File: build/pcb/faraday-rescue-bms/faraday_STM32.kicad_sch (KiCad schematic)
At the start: 58 parts, among them J1 532610571, J2 Conn_ARM_JTAG_SWD_10, J3 532610471, U2 STM32L010K8Tx, U4 THVD2410DR, Y1 ABS07-32.768KHZ-T

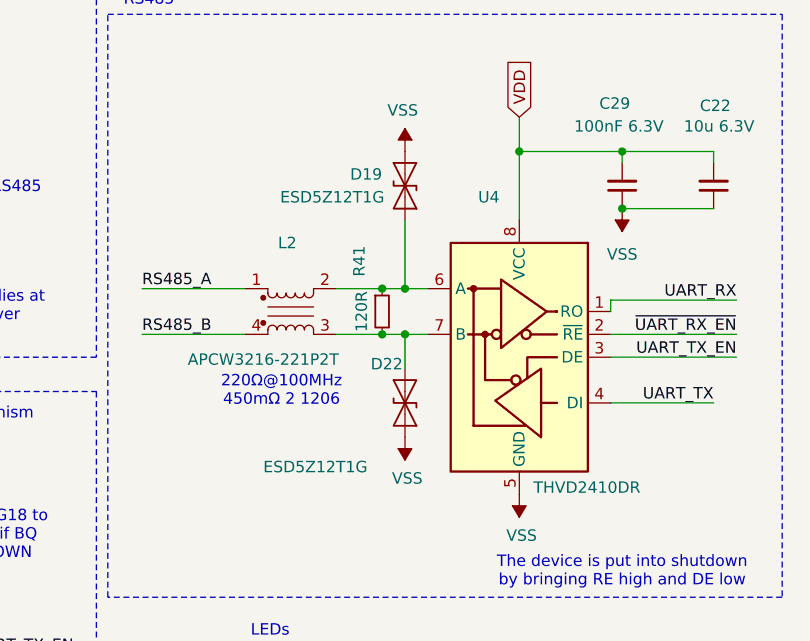
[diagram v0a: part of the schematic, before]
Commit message: Rotated diodes to fix only hardware issue.
D19 and D22 were flipped on the schematic and this propagated to the PCB. All boards from round 2 needed to be reworked to rotate D19 and D22 180deg.
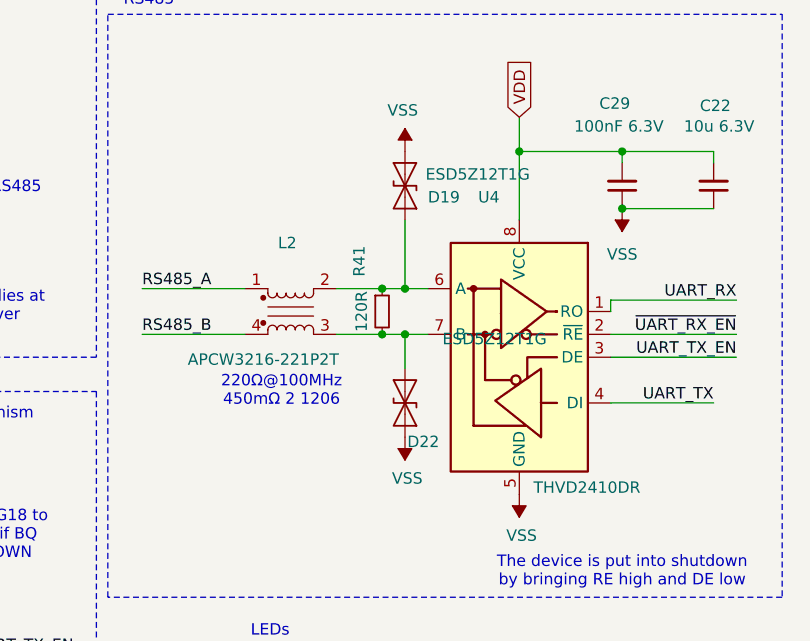
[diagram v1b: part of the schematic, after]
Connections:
- net VSS: now also D19.2 (A2), D22.2 (A2); no longer D19.1 (A1), D22.1 (A1)
- net at L2.3, R41.2, U4.7 (B): now also D22.1 (A1); no longer D22.2 (A2)
- net at L2.2, R41.1, U4.6 (A): now also D19.1 (A1); no longer D19.2 (A2)
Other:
- moved on the sheet: D19, D22
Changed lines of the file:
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@@
 	(symbol
 		(lib_id "Diode:ESD9B5.0ST5G")
-		(at 238.76 62.23 90)
+		(at 238.76 62.23 270)
 		(unit 1)
 		(exclude_from_sim no)
@@
 		(dnp no)
 		(property "Reference" "D22"
-			(at 234.95 57.912 90)
+			(at 242.57 66.548 90)
 			(effects
 				(font
@@
 		)
 		(property "Value" "ESD5Z12T1G"
-			(at 223.012 69.342 90)
+			(at 254.508 55.118 90)
 			(effects
 				(font
@@
 	(symbol
 		(lib_id "Diode:ESD9B5.0ST5G")
-		(at 238.76 38.1 270)
+		(at 238.76 38.1 90)
 		(unit 1)
 		(exclude_from_sim no)
@@
 		(dnp no)
 		(property "Reference" "D19"
-			(at 236.22 36.83 90)
+			(at 241.3 39.37 90)
 			(effects
 				(font
@@
 		)
 		(property "Value" "ESD5Z12T1G"
-			(at 236.474 39.37 90)
-			(effects
-				(font
+			(at 241.046 36.83 90)
+			(effects
+				(font
